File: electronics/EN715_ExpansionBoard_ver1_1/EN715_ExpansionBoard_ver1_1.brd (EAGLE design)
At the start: 87 x 50 mm, 46 parts, among them IC1 FE1.1S, M1 MPU9250_MODULE

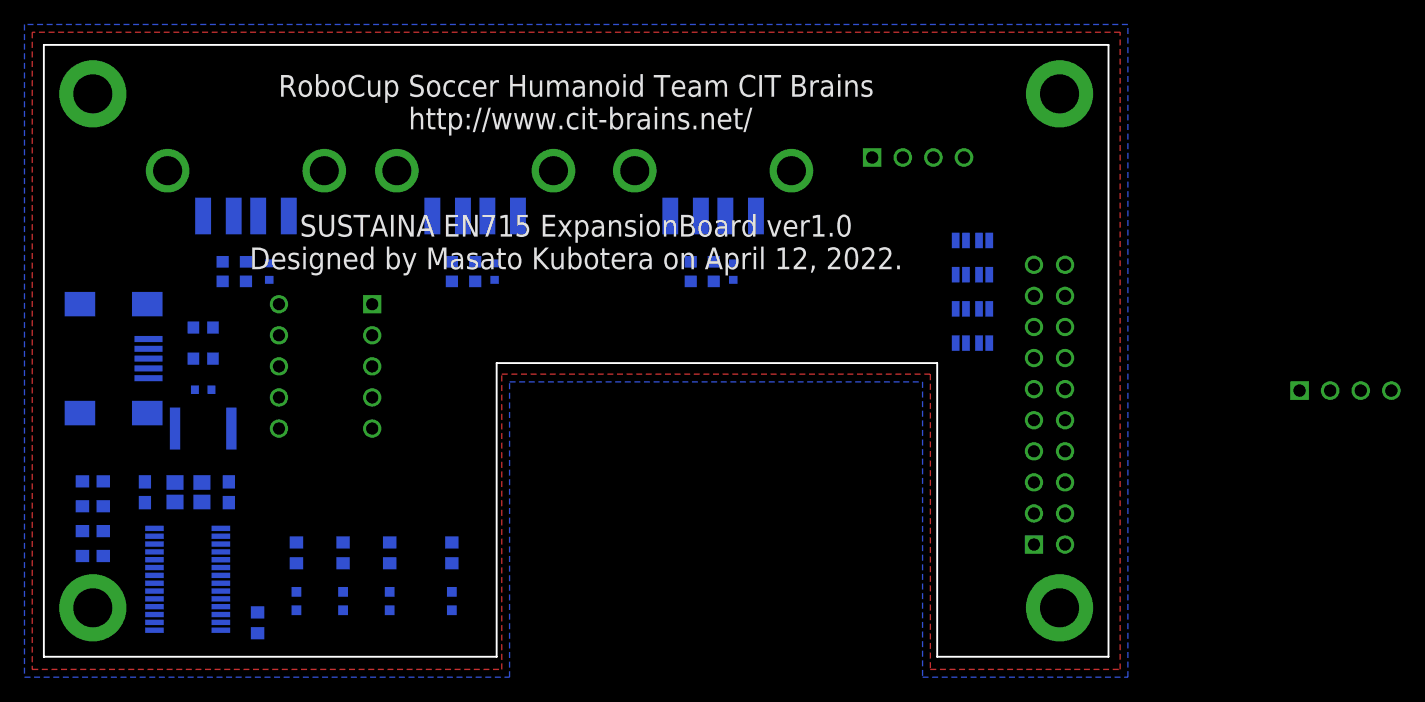
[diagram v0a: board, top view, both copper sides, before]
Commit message: Created an Expansion Board with 4 USB-HUBs
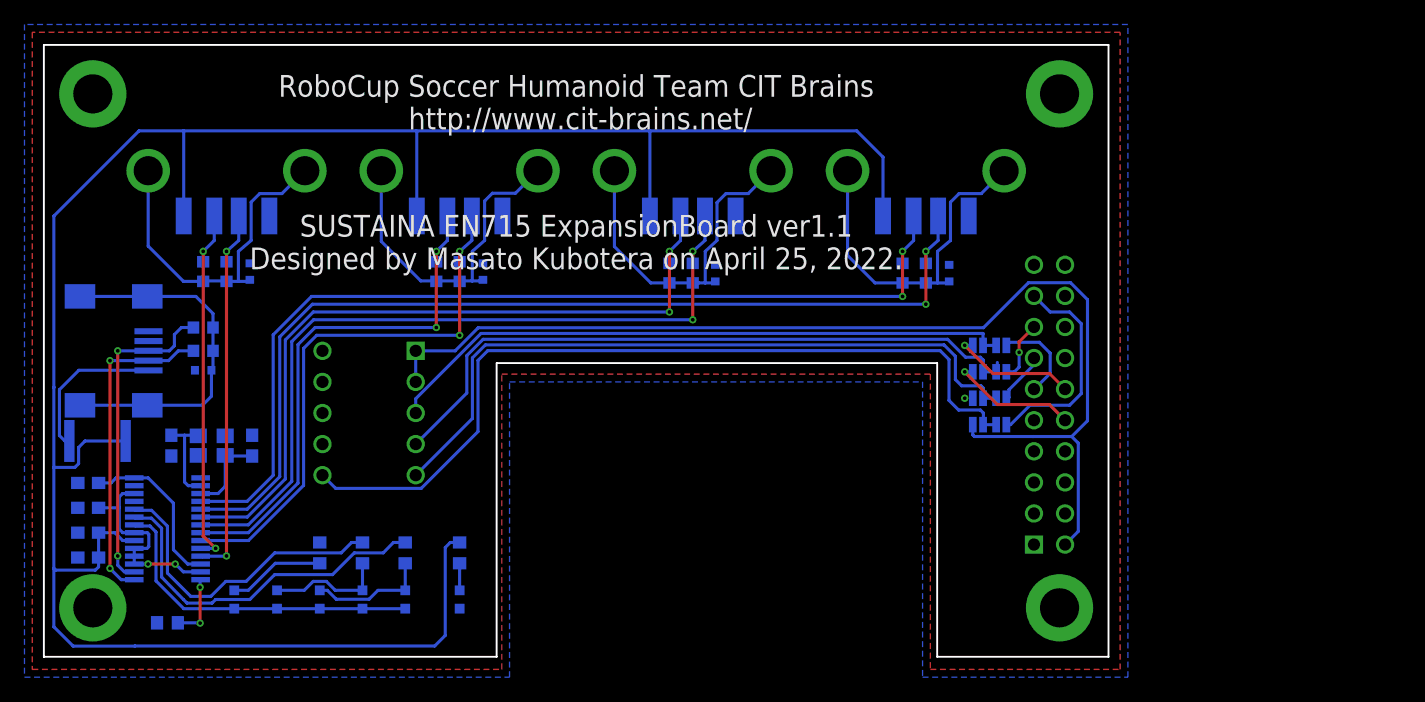
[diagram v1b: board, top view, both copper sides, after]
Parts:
- removed CH2, CH4: S4B-XH-A, JST-XH:S4B-XH-A
- added D10, D9: CG0603MLC-05E, CG0603MLC-05E:CG0603MLC-05E
- added FL5: BLM18SD220SN1D, BLM18SD220SN1D:BLM18SD220SN1D
- added LED5, LED6: (no value), led:SML0603
- added USB5: USB_A_X1_SMD, USB_Connector:USB_A_X1_SMD
- moved D3 20.3 mm to (-28.6, 6.48)
- moved D4 20.3 mm to (-30.5, 6.48)
- moved USB2 20.3 mm to (-28.6, 25.0)
- moved FL2 20.0 mm to (-26.7, 6.48)
- moved D5 17.5 mm to (-9.53, 6.48)
- moved D6 17.5 mm to (-11.4, 6.48)
- moved FL3 17.5 mm to (-7.62, 6.48)
- moved USB3 17.5 mm to (-9.53, 25.0)
- moved F1 8.70 mm to (-39.1, -7.37)
- moved JP1 8.69 mm to (34.7, 0.44)
- moved JP2 8.69 mm to (32.8, 0.44)
- moved JP3 8.06 mm to (34.7, -1.71)
- moved JP4 8.06 mm to (32.8, -1.71)
- moved JP5 7.43 mm to (34.7, -3.87)
- moved JP6 7.43 mm to (32.8, -3.87)
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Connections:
- net USB_A_2_SHIELD1 renamed USB_A_3_SHIELD
- new net USB-HUB_4_D+: D9.1, IC1.5, USB5.3
- new net USB-HUB_4_D-: D10.1, IC1.4, USB5.2
- new net USB_A_4_SHIELD: D10.2, D9.2, FL5.1, USB5.MH1, USB5.MH2
- net +3V3: no longer CH2.2, CH4.2
- net +5V: now also USB5.1
- net AGND: now also FL5.2, USB5.4; no longer CH2.1, CH4.1
- net EN715_I2C1_SCL: no longer CH4.4
- net EN715_I2C1_SDA: no longer CH4.3
- net EN715_UART2_RXD_3V3: no longer CH2.4
- net EN715_UART2_TXD_3V3: no longer CH2.3
- net FE1.1S_DRV: now also LED4.C, LED5.C, LED6.A; no longer LED4.A
- net FE1.1S_DRV_LED_A: now also LED6.C; no longer LED4.C
- net FE1.1S_LED1_A: now also LED4.A
- net FE1.1S_LED_2_A: now also LED5.A
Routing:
- net +5V: track 0.00 -> 189.7 mm
- net +3V3: track 0.00 -> 90.5 mm
- net USB-HUB_4_D+: track 0.00 -> 82.9 mm, vias 0 -> 2
- net USB-HUB_4_D-: track 0.00 -> 79.2 mm, vias 0 -> 2
- net MPU9250_CS: track 0.00 -> 68.7 mm
- net USB-HUB_3_D+: track 0.00 -> 64.4 mm, vias 0 -> 2
- net USB-HUB_3_D-: track 0.00 -> 61.1 mm, vias 0 -> 2
- net MPU9250_AD0/SD0: track 0.00 -> 58.4 mm
- net MPU9250_SDA/SDI: track 0.00 -> 55.3 mm
- net MPU9250_SCL/SCLK: track 0.00 -> 52.1 mm
- net USB-HUB_2_D+: track 0.00 -> 45.7 mm, vias 0 -> 2
- net USB-HUB_2_D-: track 0.00 -> 43.5 mm, vias 0 -> 2
- net USB-HUB_1_D+: track 0.00 -> 31.4 mm, vias 0 -> 2
- net USB-HUB_1_D-: track 0.00 -> 30.1 mm, vias 0 -> 2
- net FE1.1S_LED_1_B: track 0.00 -> 29.5 mm
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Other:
- board text added: "Port #4"
- board text added: "Port #5"
- board text added: "Power state"
- board text added: "SUSTAINA EN715 ExpansionBoard ver1.1 Designed by Masato Kubotera on April 25, 2022."
- board text added: "USB-HUB Input"
- board text added: "USB-HUB Port #1"
- board text added: "USB-HUB Port #2"
- board text added: "USB-HUB Port #3"
- board text added: "USB-HUB Port #4"
- board text removed: "3V3"
- board text removed: "GND"
- board text removed: "RXD"
- board text removed: "SCL"
- board text removed: "SDA"
- board text removed: "SUSTAINA EN715 ExpansionBoard ver1.0 Designed by Masato Kubotera on April 12, 2022."
- board text removed: "TXD"
- board text removed: "UART #2 /dev/ttyS0"
- board text removed: "USB HUB Port #1"
- board text removed: "USB HUB Port #2"
- board text removed: "USB Input state"
